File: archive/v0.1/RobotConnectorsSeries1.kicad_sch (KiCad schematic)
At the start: 8 parts

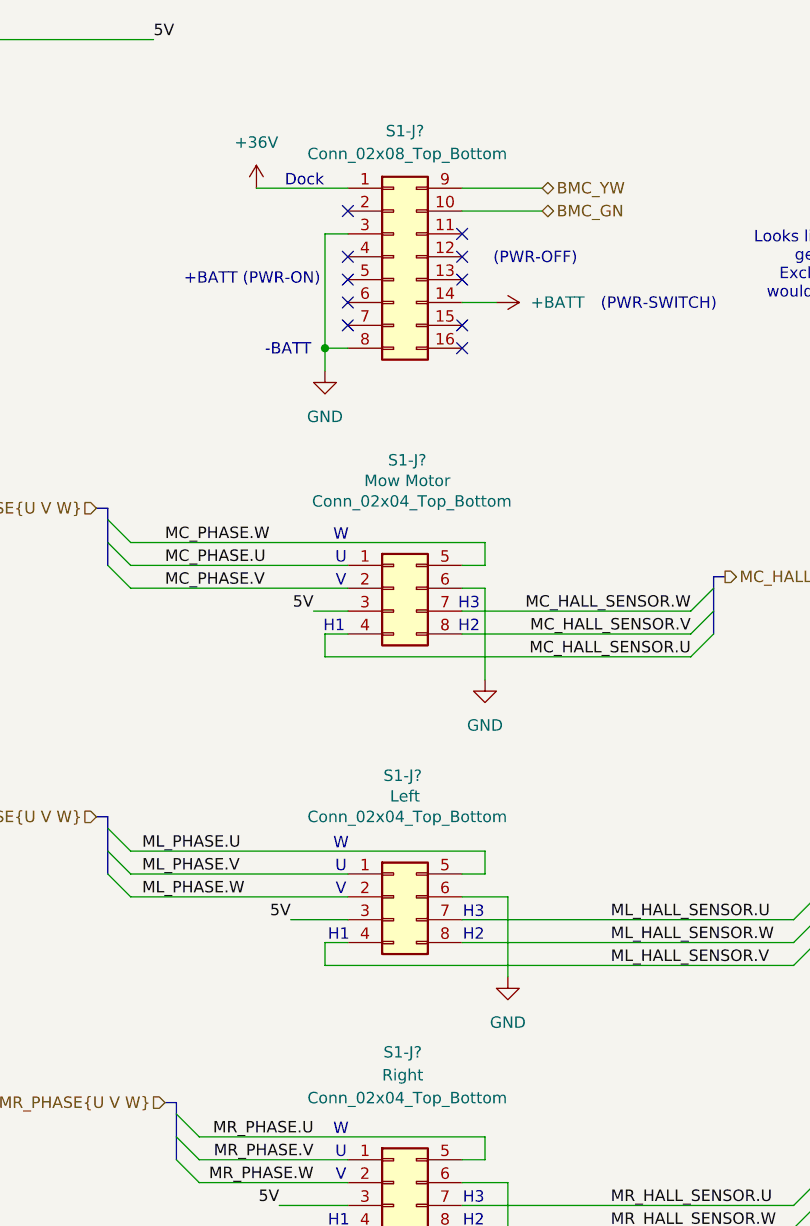
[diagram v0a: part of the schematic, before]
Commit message: Recent v0.1 and CoverUI discoveries
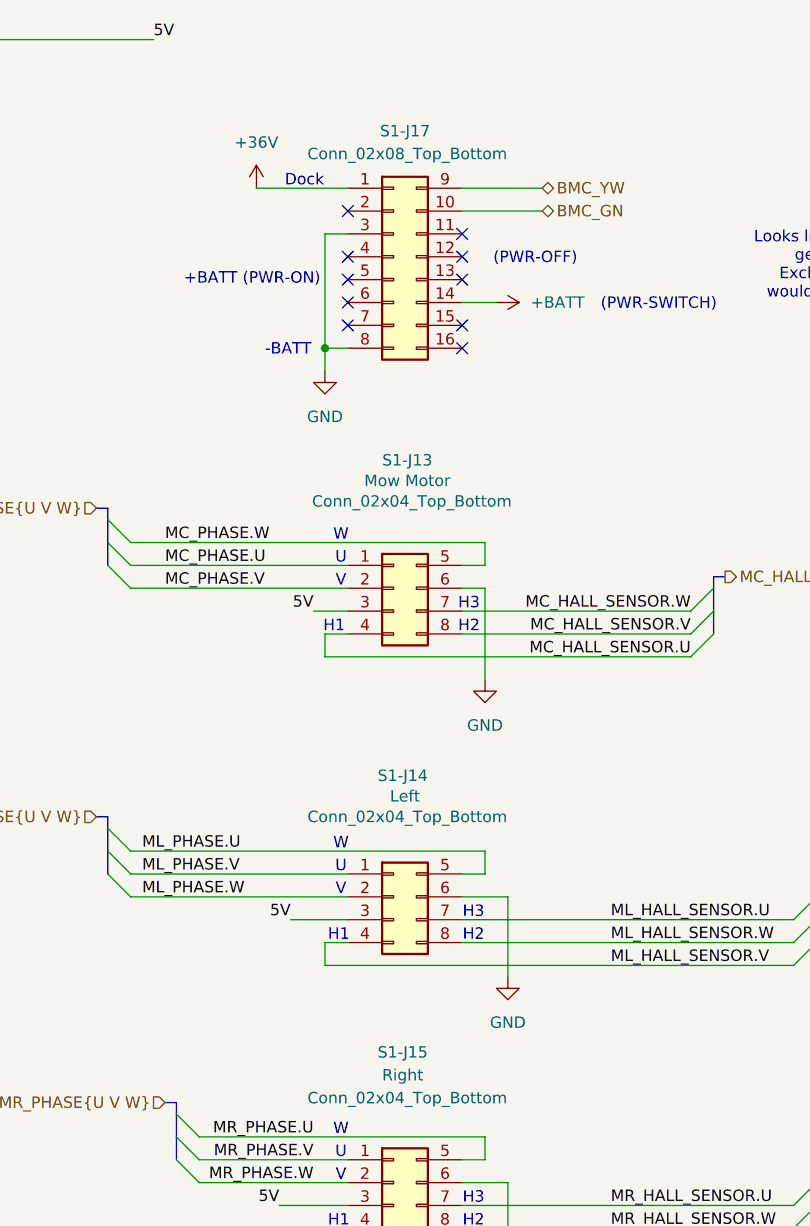
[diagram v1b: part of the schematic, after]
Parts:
- gave numbers to parts that had none: 4
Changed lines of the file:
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@@
 		(dnp no)
 		(fields_autoplaced yes)
-		(property "Reference" "#PWR?"
+		(property "Reference" "#PWR062"
 			(at 82.55 129.54 0)
 			(effects
@@
 		(on_board yes)
 		(dnp no)
-		(property "Reference" "S1-J?"
+		(property "Reference" "S1-J15"
 			(at 70.866 131.572 0)
 			(effects
@@
 		(on_board yes)
 		(dnp no)
-		(property "Reference" "S1-J?"
+		(property "Reference" "S1-J13"
 			(at 71.374 65.786 0)
 			(effects
@@
 		(dnp no)
 		(fields_autoplaced yes)
-		(property "Reference" "#PWR?"
+		(property "Reference" "#PWR065"
 			(at 62.23 62.23 0)
 			(effects
@@
 		(on_board yes)
 		(dnp no)
-		(property "Reference" "#PWR?"
+		(property "Reference" "#PWR058"
 			(at 77.47 48.26 0)
 			(effects
@@
 		(on_board yes)
 		(dnp no)
-		(property "Reference" "S1-J?"
+		(property "Reference" "S1-J14"
 			(at 70.866 100.838 0)
 			(effects
@@
 		(dnp no)
 		(fields_autoplaced yes)
-		(property "Reference" "#PWR?"
+		(property "Reference" "#PWR067"
 			(at 80.01 96.52 0)
 			(effects
@@
 		(on_board yes)
 		(dnp no)
-		(property "Reference" "#PWR?"
+		(property "Reference" "#PWR081"
 			(at 254 102.87 0)
 			(effects
@@
 		(dnp no)
 		(fields_autoplaced yes)
-		(property "Reference" "#PWR?"
+		(property "Reference" "#PWR05"
 			(at 54.61 39.37 0)
 			(effects
@@
 		(on_board yes)
 		(dnp no)
-		(property "Reference" "#PWR?"
+		(property "Reference" "#PWR080"
 			(at 245.11 50.8 0)
 			(effects
@@
 		(on_board yes)
 		(dnp no)
-		(property "Reference" "#PWR?"
+		(property "Reference" "#PWR077"
 			(at 201.93 82.55 0)
 			(effects
@@
 		(on_board yes)
 		(dnp no)
-		(property "Reference" "S1-J?"
+		(property "Reference" "S1-J17"
 			(at 71.12 29.21 0)
 			(effects
@@
 		(dnp no)
 		(fields_autoplaced yes)
-		(property "Reference" "#PWR?"
+		(property "Reference" "#PWR06"
 			(at 82.55 161.29 0)
 			(effects
@@
 		(on_board yes)
 		(dnp no)
-		(property "Reference" "#PWR?"
+		(property "Reference" "#PWR075"
 			(at 184.15 82.55 0)
 			(effects
